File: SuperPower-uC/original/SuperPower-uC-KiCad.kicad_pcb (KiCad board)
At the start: 2 copper layers, 95 x 42 mm, 169 parts, among them J1 JST_PH_S2B_thru, J2 Barrel_Jack_Switch, J3 Conn_01x02_Male, J4 DNP/JST_ZH_S2B_thru, J5 JST_XH_S2B_thru, J6 Conn_01x02_Male, J7 mcu_pinout, J8 mcu_pinout, Q1 DMN2019UTS, Q10 2N7002A, Q11 2N7002A, Q12 DMP2035UVT, Q13 DMP2035UVT, Q14 DMP2035UVT, Q2 DMP3028LSD, Q3 DMN3018SSD, Q4 2N7002A, Q5 DMP2035UVT, Q6 BSS84-7-F, Q7 S8050, Q8 S8050, Q9 2N7002A, SW1 DNP/SKRKAEE020, U1 AP9101CK6-AYTRG1, U10 TPS63070RNMT, U2 USB-C, U3 IP4220CZ6, U4 LTC4162EUFD-LAD, U5 RV-3028-C7, U6 CP2102N-A01-GQFN28, U7 ESP32-WROOM32, U8 TPS70933DRVT, U9 TPS63070RNMT

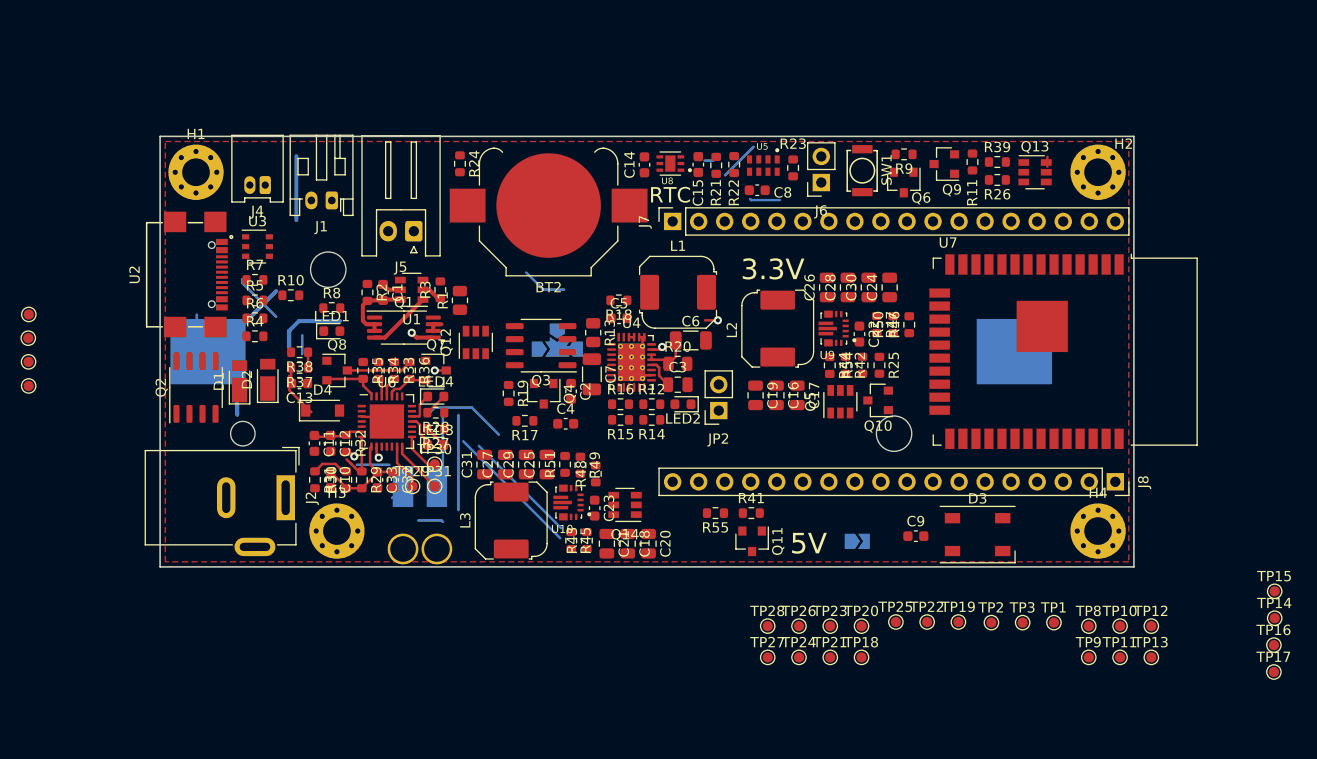
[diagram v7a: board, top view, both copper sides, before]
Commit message: Update Single rows Headers to be fully compatible with ESP WROOM modules
(ESP-32 DevKit C rev. 4)
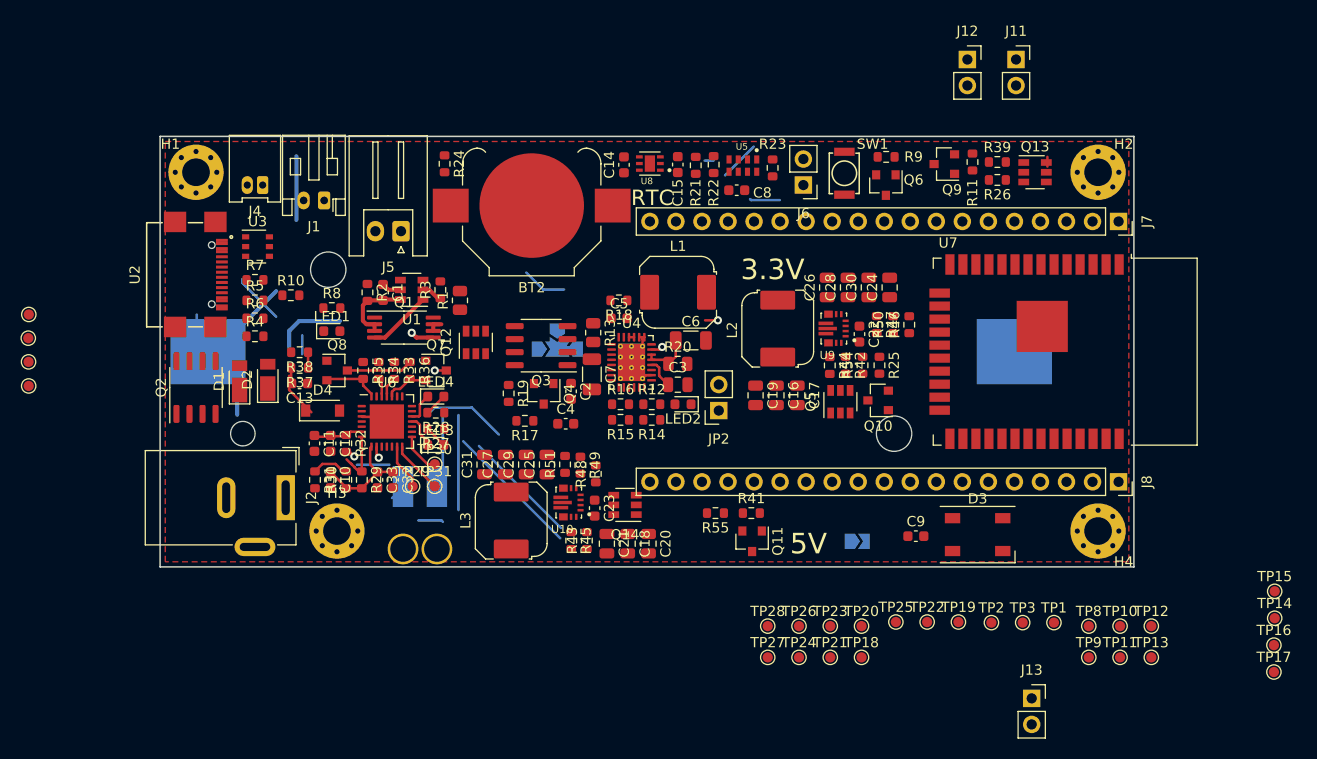
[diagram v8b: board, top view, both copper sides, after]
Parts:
- added J11: Conn_01x02_Male, Connector_PinSocket_2.54mm:PinSocket_1x02_P2.54mm_Vertical, F.Cu at (193.5, 26.5)
- added J12: Conn_01x02_Male, Connector_PinSocket_2.54mm:PinSocket_1x02_P2.54mm_Vertical, F.Cu at (188.8, 26.5)
- added J13: Conn_01x02_Male, Connector_PinSocket_2.54mm:PinSocket_1x02_P2.54mm_Vertical, F.Cu at (195.0, 88.8)
- J6: footprint Connector_PinSocket_2.54mm:PinSocket_1x02_P2.54mm_Vertical -> Connector_PinHeader_2.54mm:PinHeader_1x02_P2.54mm_Vertical
- J7, J8: value mcu_pinout -> Conn_01x19_Female; footprint Connector_PinSocket_2.54mm:PinSocket_1x18_P2.54mm_Vertical -> Connector_PinSocket_2.54mm:PinSocket_1x19_P2.54mm_Vertical
- moved J7 43.5 mm to (203.5, 42.3), turned to 270 degrees
- moved C14 2.00 mm to (155.2, 36.8)
- moved C15 2.00 mm to (160.5, 36.8)
- moved C8 2.00 mm to (166.2, 39.2)
- moved R21 2.00 mm to (162.2, 36.8)
- moved R22 2.00 mm to (164.0, 36.8)
- moved R23 2.00 mm to (169.8, 37.1)
- moved U5 2.00 mm to (166.8, 36.9)
- moved U8 2.00 mm to (157.8, 36.6)
- moved J6 1.77 mm to (172.8, 38.8)
- moved Q6 1.77 mm to (180.8, 38.8)
- moved R9 1.77 mm to (180.8, 36.0)
- moved SW1 1.77 mm to (176.8, 37.6)
- moved BT2 1.65 mm to (146.2, 40.8)
- moved R24 1.50 mm to (137.8, 36.7)
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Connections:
- J7 pad 1: /MCU Module/5V -> /MCU Module/3v3_MCU
- J7 pad 10: /MCU Module/IO25 -> /MCU Module/IO26
- J7 pad 11: /MCU Module/IO33 -> /MCU Module/IO27
- J7 pad 12: /~SMBALERT -> /MCU Module/IO14
- J7 pad 13: /MCU Module/IO35 -> /MCU Module/EN_3V3
- J7 pad 14: /MCU Module/IO34 -> GND
- J7 pad 15: /MCU Module/IO39 -> /MCU Module/EN_5V
- J7 pad 16: /MCU Module/IO36 -> /MCU Module/SD2
- J7 pad 17: /MCU Module/EN -> /MCU Module/SD3
- J7 pad 18: GND -> /MCU Module/CMD
- J7 pad 2: GND -> /MCU Module/EN
- J7 pad 3: /VBUS1 -> /MCU Module/IO36
- J7 pad 4: GND -> /MCU Module/IO39
- J7 pad 5: /MCU Module/EN_5V -> /MCU Module/IO34
- J7 pad 6: /MCU Module/EN_3V3 -> /MCU Module/IO35
- J7 pad 7: /MCU Module/IO14 -> /~SMBALERT
- J7 pad 8: /MCU Module/IO27 -> /MCU Module/IO33
- J7 pad 9: /MCU Module/IO26 -> /MCU Module/IO25
- J8 pad 1: /MCU Module/IO0 -> GND
- J8 pad 10: /MCU Module/IO17 -> /MCU Module/IO5
- J8 pad 11: /MCU Module/IO16 -> /MCU Module/IO17
- J8 pad 12: /MCU Module/IO4 -> /MCU Module/IO16
- J8 pad 13: /MCU Module/RGBW_LED -> /MCU Module/IO4
- J8 pad 14: /MCU Module/IO15 -> /MCU Module/IO0
- J8 pad 15: GND -> /MCU Module/RGBW_LED
- J8 pad 16: /MCU Module/3v3_MCU -> /MCU Module/IO15
- J8 pad 17: GND -> /MCU Module/SD1
- J8 pad 18: /MCU Module/3v3 -> /MCU Module/SD0
- J8 pad 7: /MCU Module/IO19 -> GND
- J8 pad 8: /MCU Module/IO18 -> /MCU Module/IO19
- J8 pad 9: /MCU Module/IO5 -> /MCU Module/IO18
- U7 pad 17: Net-(U7-Pad17) -> /MCU Module/SD2
- U7 pad 18: Net-(U7-Pad18) -> /MCU Module/SD3
- U7 pad 19: Net-(U7-Pad19) -> /MCU Module/CMD
- U7 pad 20: Net-(U7-Pad20) -> /MCU Module/CLK
- U7 pad 21: Net-(U7-Pad21) -> /MCU Module/SD0
- U7 pad 22: Net-(U7-Pad22) -> /MCU Module/SD1
